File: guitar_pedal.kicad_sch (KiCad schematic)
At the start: 114 parts, among them J1 Conn_01x02_Pin, J2 Conn_01x02_Pin, J3 Conn_01x02_Pin, Q1 2N3904, Q2 2N3904, Q3 2N3904, Q4 2N3904, Q5 2N3904, U1 LM358, U2 LM358, U3 LM358, U4 LM358, U5 LM358

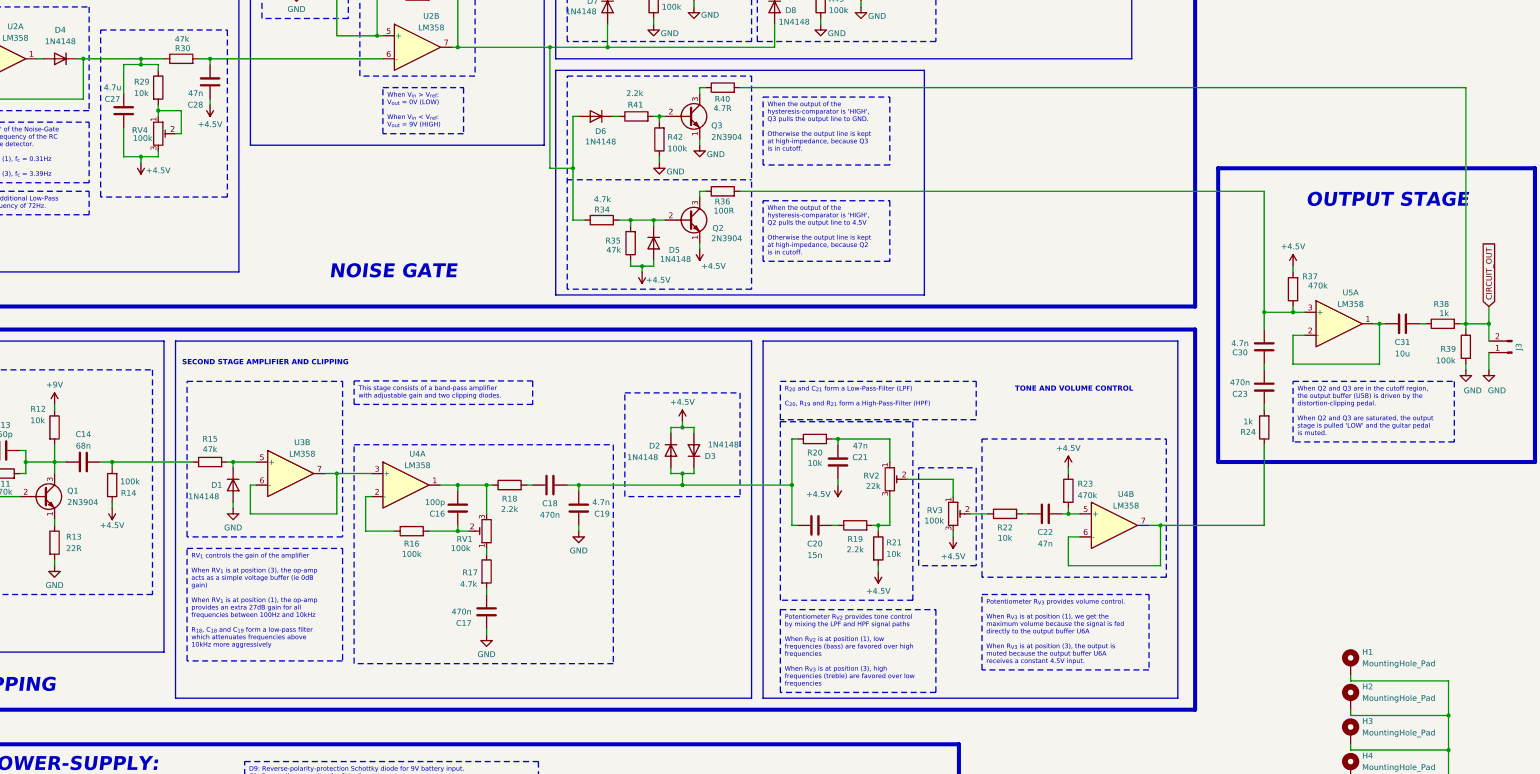
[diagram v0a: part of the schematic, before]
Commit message: replaced ceramic capacitors with polyester. Added stitching vias between top and bottom ground planes
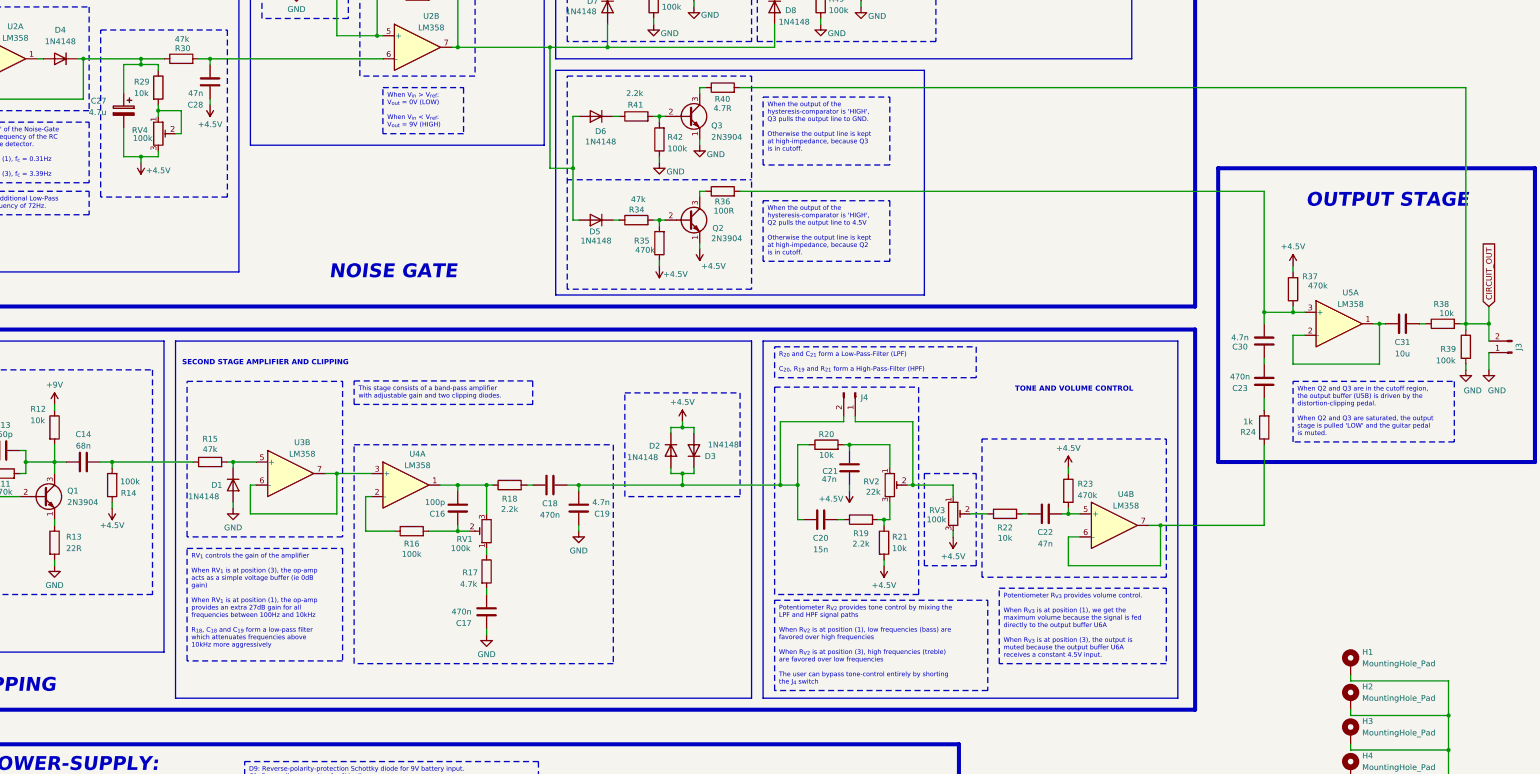
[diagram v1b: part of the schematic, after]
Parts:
- removed C27: 4.7u, Capacitor_THT:C_Disc_D6.0mm_W2.5mm_P5.00mm, symbol Device:C
- added C27: 4.7u, Capacitor_THT:CP_Radial_D5.0mm_P2.50mm, symbol Device:C_Polarized
- added J4: Conn_01x02_Pin, Connector_PinHeader_2.54mm:PinHeader_1x02_P2.54mm_Vertical, symbol Connector:Conn_01x02_Pin
- C10, C12, C14, C15, C19, C20, C21, C22, C25, C28, C29, C3, C30, C5, C6, C8, C9: footprint Capacitor_THT:C_Disc_D6.0mm_W2.5mm_P5.00mm -> Capacitor_THT:C_Rect_L7.2mm_W2.5mm_P5.00mm_FKS2_FKP2_MKS2_MKP2
- C11, C17, C18, C23, C24: footprint Capacitor_THT:C_Disc_D6.0mm_W2.5mm_P5.00mm -> Capacitor_THT:C_Rect_L7.2mm_W3.5mm_P5.00mm_FKS2_FKP2_MKS2_MKP2
- D10, D11, D12: footprint LED_THT:LED_D5.0mm -> Connector_PinHeader_2.54mm:PinHeader_1x02_P2.54mm_Vertical
- R34: value 4.7k -> 47k
- R35: value 47k -> 470k
- R38: value 1k -> 10k
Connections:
- net +4.5V: now also C27.2; no longer D5.2 (A)
- net at C18.2, C19.2, C20.1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: now also J4.2 (Pin_2)
- net at D4.1 (K), R29.1, R30.1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: now also C27.1
- net at Q2.2 (B), R34.2, R35.2: no longer D5.1 (K)
- net at D6.2 (A), D7.2 (A), D8.2 (A)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: now also D5.2 (A); no longer R34.1
- net at RV2.2, RV3.1: now also J4.1 (Pin_1)
- new net: D5.1 (K), R34.1
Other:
- moved on the sheet: C20, C21, C23, C30, D5, R19, R20, R21, R34, R35, RV2

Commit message: drop files from .gitignore
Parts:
- C1, C2, C4: footprint Capacitor_THT:CP_Radial_D5.0mm_P2.50mm -> Capacitor_THT:CP_Radial_D6.3mm_P2.50mm; KiLib_Generator (none) -> capacitor/THT/other
- C10, C11, C12, C13, C14, C15, C16, C17, C18, C19, C20, C21, C22, C23, C24, C25, C26, C27, C28, C29, C3, C30, C31, C5, C6, C7, C8, C9: KiLib_Generator (none) -> capacitor/THT/other
- D1, D2, D3, D4, D5, D6, D7, D8, D9: KiLib_Generator (none) -> diode/THT
- H1, H2, H3, H4: KiLib_Generator (none) -> mounting_hardware/mounting_hole
- J1, J2, J3, J4, RV1, RV2, RV3, RV4, RV5: KiLib_Generator (none) -> connector/pin_header_socket
- LED1: renamed from D12; KiLib_Generator (none) -> connector/pin_header_socket
- LED2: renamed from D11; KiLib_Generator (none) -> connector/pin_header_socket
- LED3: renamed from D10; KiLib_Generator (none) -> connector/pin_header_socket
- R1, R10, R11, R12, R13, R14, R15, R16, R17, R18, R19, R2, R20, R21, R22, R23, R24, R25, R26, R27, R28, R29, R3, R30, R31, R32, R33, R34, R35, R36, R37, R38, R39, R4, R40, R41, R42, R43, R44, R45, R46, R47, R48, R49, R5, R6, R7, R8, R9: KiLib_Generator (none) -> resistor/THT
- U1, U2, U3, U4, U5: KiLib_Generator (none) -> package/DIP/legacy
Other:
- moved on the sheet: C4, C5, C7, C8, J2, R12, R24, R4, R5

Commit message: fixed pull-downn lines for noise gate
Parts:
- R36: value 100R -> 10R
- R38: value 10k -> 1k
- R43, R45, R47: value 2.2k -> 10k
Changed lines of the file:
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@@
 			)
 		)
-		(property "Value" "2.2k"
+		(property "Value" "10k"
 			(at 378.968 45.466 0)
 			(show_name no)
@@
 			)
 		)
-		(property "Value" "2.2k"
+		(property "Value" "10k"
 			(at 202.692 256.032 0)
 			(show_name no)
@@
 			)
 		)
-		(property "Value" "2.2k"
+		(property "Value" "10k"
 			(at 345.186 38.354 90)
 			(show_name no)
@@
 			)
 		)
-		(property "Value" "100R"
+		(property "Value" "10R"
 			(at 352.298 107.188 90)
 			(show_name no)
@@
 			)
 		)
-		(property "Value" "10k"
+		(property "Value" "1k"
 			(at 511.048 129.794 90)
 			(show_name no)
